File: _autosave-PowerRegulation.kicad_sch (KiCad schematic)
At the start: 29 parts, among them J5 XT60-M, K1 PR30-24V-450-1A, Q7 BSS138, U6 TPS5430DDA, U7 TPS5430DDA, U8 XC6206P332MR

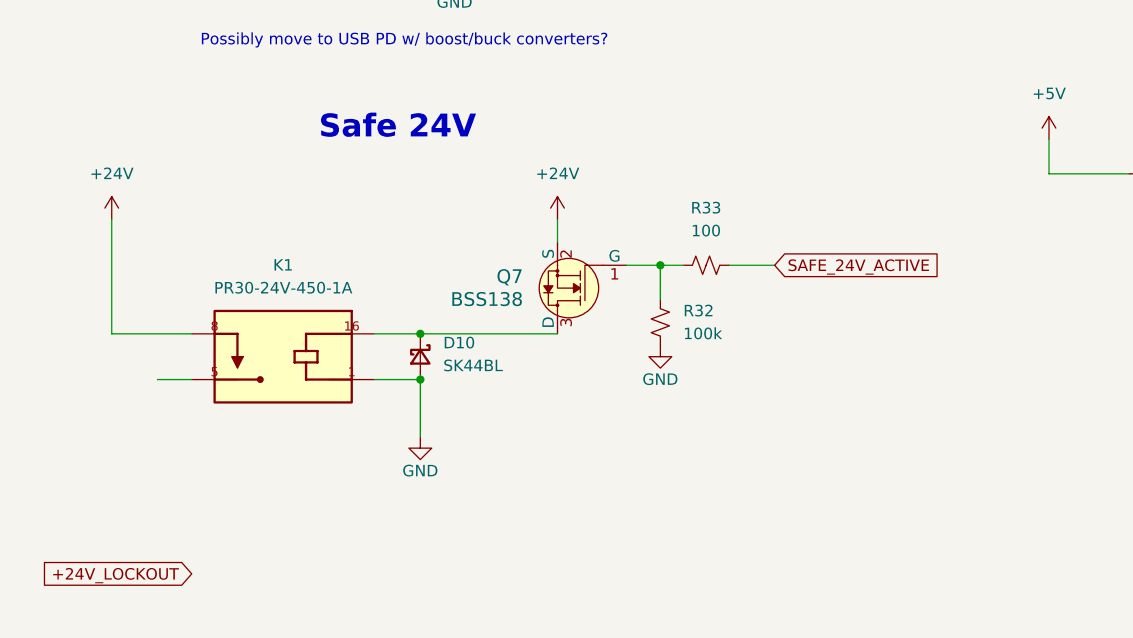
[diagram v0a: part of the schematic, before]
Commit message: Add SAFE +24V
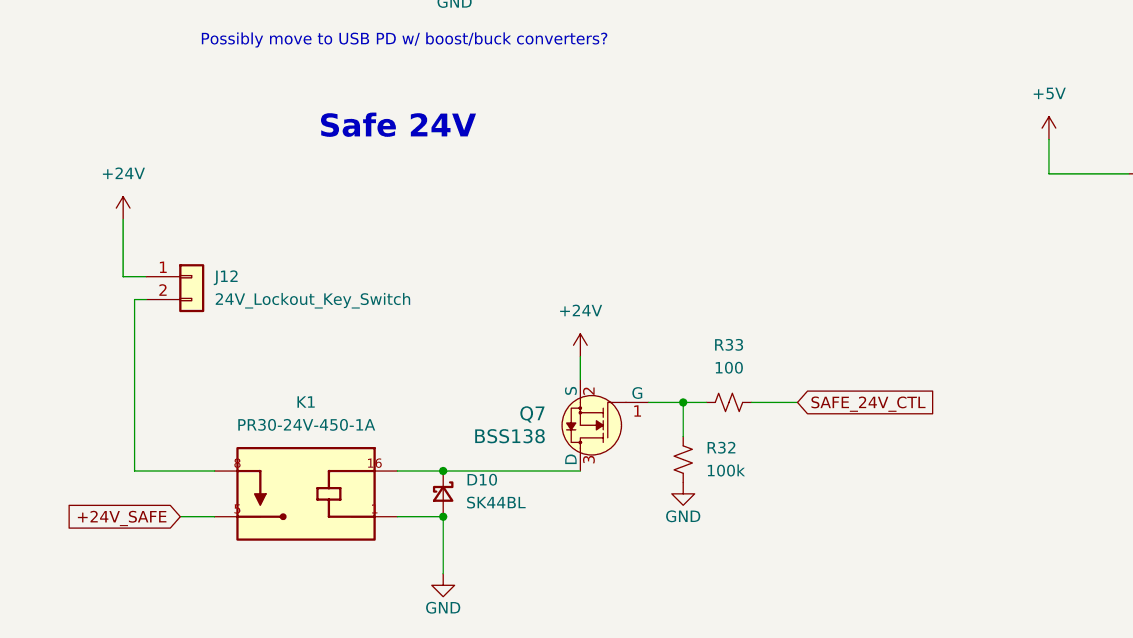
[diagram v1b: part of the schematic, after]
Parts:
- added J12: 24V_Lockout_Key_Switch, Connector_JST:JST_XH_B2B-XH-A_1x02_P2.50mm_Vertical, symbol Connector_Generic:Conn_01x02
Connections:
- net +24V: now also J12.1 (Pin_1); no longer K1.8
- net +24V_SAFE: now reaches K1.5
- net SAFE_24V_ACTIVE renamed SAFE_24V_CTL
- new net: J12.2 (Pin_2), K1.8
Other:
- moved on the sheet: D10, K1, Q7, R32, R33
